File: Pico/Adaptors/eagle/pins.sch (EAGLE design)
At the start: 4 parts

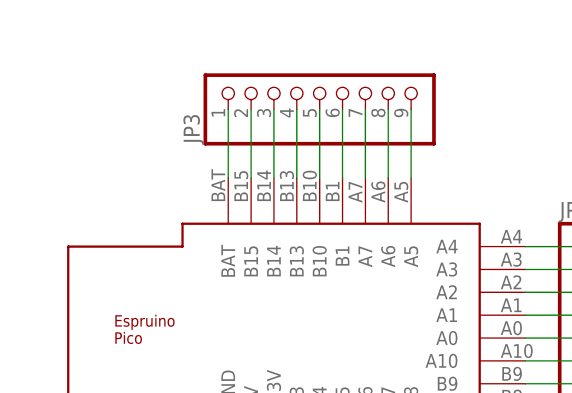
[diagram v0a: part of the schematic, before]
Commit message: add JST connector to pins, update thumbnails
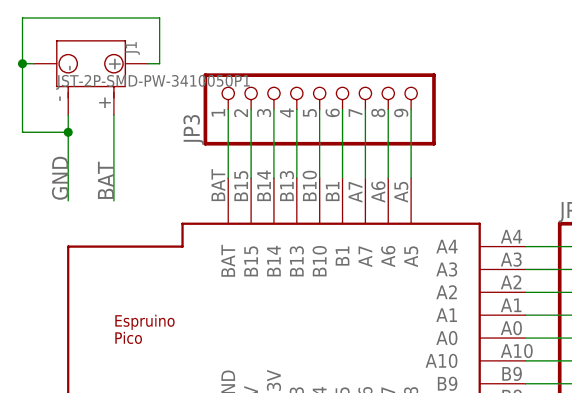
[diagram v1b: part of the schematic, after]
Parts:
- added J1: JST-2P-SMD-PW-3410050P1, OPL Eagle Library:JST-2P-SMD-PW-3410050P1
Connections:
- removed net N$15: JP3.1, U$1.BAT
- new net BAT: J1.+, JP3.1, U$1.BAT
- net GND: now also J1.-, J1.3, J1.4
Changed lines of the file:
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@@
 <layers>
 <layer number="1" name="Top" color="4" fill="1" visible="no" active="no"/>
+<layer number="2" name="Route2" color="1" fill="3" visible="no" active="no"/>
+<layer number="15" name="Route15" color="4" fill="6" visible="no" active="no"/>
 <layer number="16" name="Bottom" color="1" fill="1" visible="no" active="no"/>
 <layer number="17" name="Pads" color="2" fill="1" visible="no" active="no"/>
@@
 <layer number="48" name="Document" color="7" fill="1" visible="no" active="no"/>
 <layer number="49" name="Reference" color="7" fill="1" visible="no" active="no"/>
+<layer number="50" name="dxf" color="7" fill="1" visible="no" active="no"/>
 <layer number="51" name="tDocu" color="7" fill="1" visible="no" active="no"/>
 <layer number="52" name="bDocu" color="7" fill="1" visible="no" active="no"/>
+<layer number="53" name="tGND_GNDA" color="7" fill="9" visible="no" active="no"/>
+<layer number="54" name="bGND_GNDA" color="1" fill="9" visible="no" active="no"/>
+<layer number="56" name="wert" color="7" fill="1" visible="no" active="no"/>
 <layer number="91" name="Nets" color="2" fill="1" visible="yes" active="yes"/>
 <layer number="92" name="Busses" color="1" fill="1" visible="yes" active="yes"/>
@@
 <layer number="97" name="Info" color="7" fill="1" visible="yes" active="yes"/>
 <layer number="98" name="Guide" color="6" fill="1" visible="yes" active="yes"/>
+<layer number="100" name="Muster" color="7" fill="1" visible="no" active="no"/>
+<layer number="101" name="Patch_Top" color="12" fill="4" visible="no" active="no"/>
+<layer number="102" name="Vscore" color="7" fill="1" visible="no" active="no"/>
+<layer number="103" name="tMap" color="7" fill="1" visible="no" active="no"/>
+<layer number="104" name="Name" color="7" fill="1" visible="no" active="no"/>
+<layer number="105" name="tPlate" color="7" fill="1" visible="no" active="no"/>
+<layer number="106" name="bPlate" color="7" fill="1" visible="no" active="no"/>
+<layer number="107" name="Crop" color="7" fill="1" visible="no" active="no"/>
+<layer number="108" name="fp8" color="7" fill="1" visible="no" active="no"/>
+<layer number="109" name="fp9" color="7" fill="1" visible="no" active="no"/>
+<layer number="110" name="110" color="7" fill="1" visible="no" active="no"/>
+<layer number="111" name="111" color="7" fill="1" visible="no" active="no"/>
+<layer number="112" name="tSilk" color="7" fill="1" visible="no" active="no"/>
+<layer number="116" name="Patch_BOT" color="9" fill="4" visible="no" active="no"/>
+<layer number="118" name="Rect_Pads" color="7" fill="1" visible="no" active="no"/>
+<layer number="121" name="_tsilk" color="7" fill="1" visible="no" active="no"/>
+<layer number="122" name="_bsilk" color="7" fill="1" visible="no" active="no"/>
+<layer number="123" name="tTestmark" color="7" fill="1" visible="no" active="no"/>
+<layer number="124" name="bTestmark" color="7" fill="1" visible="no" active="no"/>
+<layer number="125" name="_tNames" color="7" fill="1" visible="no" active="no"/>
+<layer number="126" name="_bNames" color="7" fill="1" visible="no" active="no"/>
+<layer number="127" name="_tValues" color="7" fill="1" visible="no" active="no"/>
+<layer number="128" name="_bValues" color="7" fill="1" visible="no" active="no"/>
+<layer number="131" name="tAdjust" color="7" fill="1" visible="no" active="no"/>
+<layer number="132" name="bAdjust" color="7" fill="1" visible="no" active="no"/>
+<layer number="144" name="DrillLegend" color="7" fill="1" visible="no" active="no"/>
+<layer number="151" name="HeatSink" color="14" fill="1" visible="no" active="no"/>
+<layer number="152" name="_bDocu" color="7" fill="1" visible="no" active="no"/>
+<layer number="199" name="Contour" color="7" fill="1" visible="no" active="no"/>
+<layer number="200" name="200bmp" color="1" fill="10" visible="no" active="no"/>
+<layer number="201" name="201bmp" color="2" fill="1" visible="no" active="no"/>
+<layer number="202" name="202bmp" color="3" fill="1" visible="no" active="no"/>
+<layer number="203" name="203bmp" color="4" fill="10" visible="no" active="no"/>
+<layer number="204" name="204bmp" color="5" fill="10" visible="no" active="no"/>
+<layer number="205" name="205bmp" color="6" fill="10" visible="no" active="no"/>
+<layer number="206" name="206bmp" color="7" fill="10" visible="no" active="no"/>
+<layer number="207" name="207bmp" color="15" fill="10" visible="no" active="no"/>
+<layer number="208" name="208bmp" color="9" fill="10" visible="no" active="no"/>
+<layer number="209" name="209bmp" color="7" fill="1" visible="no" active="no"/>
+<layer number="210" name="210bmp" color="7" fill="1" visible="no" active="no"/>
+<layer number="211" name="211bmp" color="7" fill="1" visible="no" active="no"/>
+<layer number="212" name="212bmp" color="7" fill="1" visible="no" active="no"/>
+<layer number="213" name="213bmp" color="7" fill="1" visible="no" active="no"/>
+<layer number="214" name="214bmp" color="7" fill="1" visible="no" active="no"/>
+<layer number="215" name="215bmp" color="7" fill="1" visible="no" active="no"/>
+<layer number="216" name="216bmp" color="7" fill="1" visible="no" active="no"/>
+<layer number="217" name="217bmp" color="18" fill="1" visible="no" active="no"/>
+<layer number="218" name="218bmp" color="19" fill="1" visible="no" active="no"/>
+<layer number="219" name="219bmp" color="20" fill="1" visible="no" active="no"/>
+<layer number="220" name="220bmp" color="21" fill="1" visible="no" active="no"/>
+<layer number="221" name="221bmp" color="22" fill="1" visible="no" active="no"/>
+<layer number="222" name="222bmp" color="23" fill="1" visible="no" active="no"/>
+<layer number="223" name="223bmp" color="24" fill="1" visible="no" active="no"/>
+<layer number="224" name="224bmp" color="25" fill="1" visible="no" active="no"/>
+<layer number="248" name="Housing" color="7" fill="1" visible="no" active="no"/>
+<layer number="249" name="Edge" color="7" fill="1" visible="no" active="no"/>
+<layer number="250" name="Descript" color="3" fill="1" visible="no" active="no"/>
+<layer number="251" name="SMDround" color="12" fill="11" visible="no" active="no"/>
+<layer number="254" name="OrgLBR" color="13" fill="1" visible="no" active="no"/>
 </layers>
 <schematic xreflabel="%F%N/%S.%C%R" xrefpart="/%S.%C%R">
@@
 <part name="JP3" library="pinhead-2" deviceset="PINHD-1X09" device="_2.54-S"/>
 <part name="JP4" library="pinhead-2" deviceset="PINHD-1X09" device="_2.54-S"/>
+<part name="J1" library="OPL Eagle Library" deviceset="JST-2P-SMD-PW" device="-3410050P1"/>
 </parts>
 <sheets>
@@
 <instance part="JP3" gate="A" x="40.64" y="38.1" rot="R90"/>
 <instance part="JP4" gate="A" x="40.64" y="-17.78" rot="MR270"/>
+<instance part="J1" gate="J" x="15.24" y="40.64" rot="R270"/>
 </instances>
 <busses>
@@
 <wire x1="30.48" y1="-5.08" x2="30.48" y2="-15.24" width="0.1524" layer="91"/>
 </segment>
+<segment>
+<wire x1="21.59" y1="40.64" x2="22.86" y2="40.64" width="0.1524" layer="91"/>
+<wire x1="22.86" y1="40.64" x2="22.86" y2="45.72" width="0.1524" layer="91"/>
+<wire x1="12.7" y1="34.925" x2="12.7" y2="33.02" width="0.1524" layer="91"/>
+<wire x1="12.7" y1="33.02" x2="12.7" y2="25.4" width="0.1524" layer="91"/>
+<wire x1="8.89" y1="40.64" x2="7.62" y2="40.64" width="0.1524" layer="91"/>
+<wire x1="7.62" y1="40.64" x2="7.62" y2="33.02" width="0.1524" layer="91"/>
+<wire x1="7.62" y1="33.02" x2="12.7" y2="33.02" width="0.1524" layer="91"/>
+<wire x1="22.86" y1="45.72" x2="7.62" y2="45.72" width="0.1524" layer="91"/>
+<wire x1="7.62" y1="45.72" x2="7.62" y2="40.64" width="0.1524" layer="91"/>
+<junction x="12.7" y="33.02"/>
+<junction x="7.62" y="40.64"/>
+<label x="12.7" y="25.4" size="1.778" layer="95" rot="R90"/>
+<pinref part="J1" gate="J" pin="-"/>
+<pinref part="J1" gate="J" pin="3"/>
+<pinref part="J1" gate="J" pin="4"/>
+</segment>
 </net>
 <net name="N$9" class="0">
@@
 </segment>
 </net>
-<net name="N$15" class="0">
+<net name="BAT" class="0">
 <segment>
 <pinref part="U$1" gate="G$1" pin="BAT"/>
@@
 <wire x1="30.48" y1="27.94" x2="30.48" y2="35.56" width="0.1524" layer="91"/>
 </segment>
-</net>
+<segment>
+<label x="17.78" y="25.4" size="1.778" layer="95" rot="R90"/>
+<pinref part="J1" gate="J" pin="+"/>
+<wire x1="17.78" y1="34.925" x2="17.78" y2="25.4" width="0.1524" layer="91"/>
+</segment>
+</net>

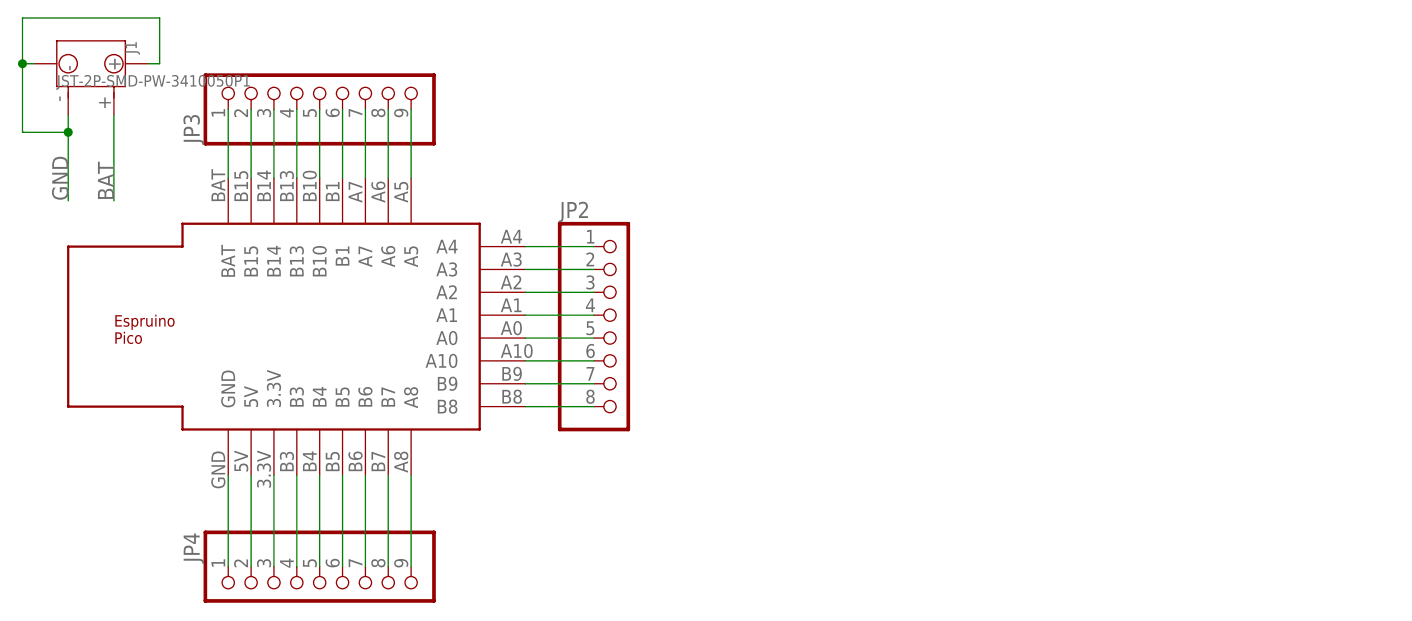
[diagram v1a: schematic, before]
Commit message: Added battery charger pads to proto headers
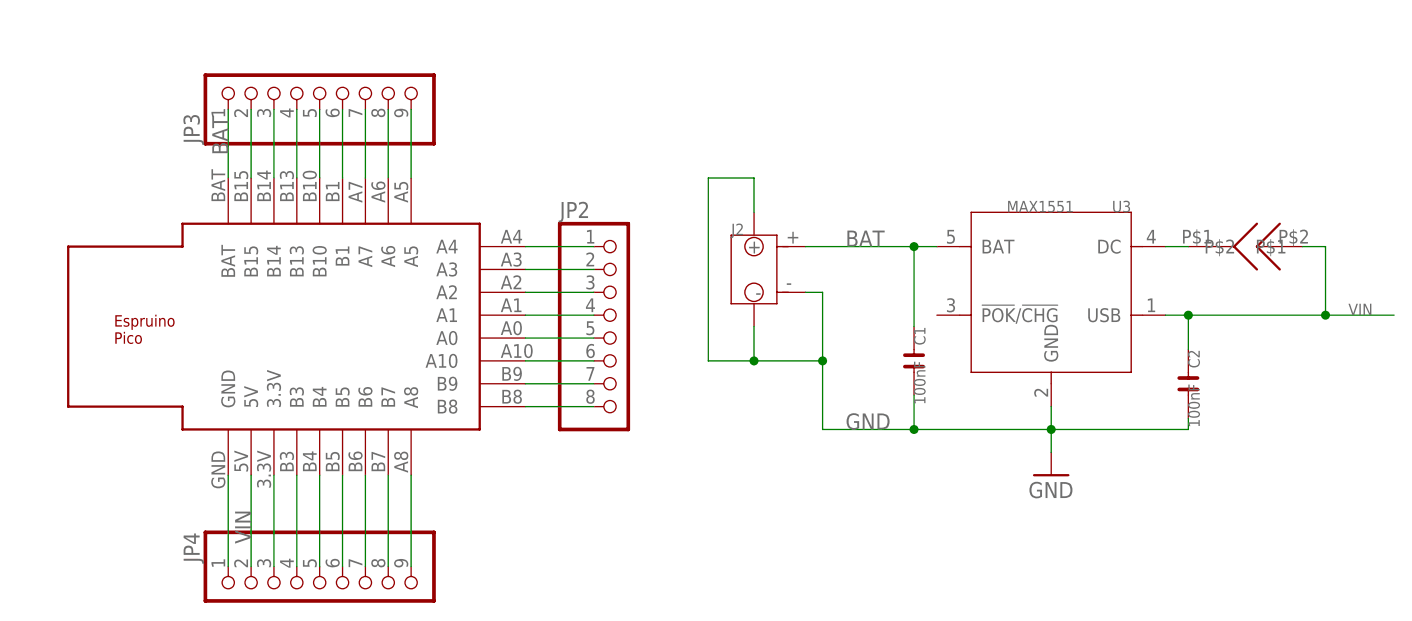
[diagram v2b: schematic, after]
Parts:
- removed J1: JST-2P-SMD-PW-3410050P1, OPL Eagle Library:JST-2P-SMD-PW-3410050P1
- added C1, C2: 100nF, OPL5:C-0603
- added J2: JST-2P-SMD-PW-3410050P1, OPL Eagle Library:JST-2P-SMD-PW-3410050P1
- added U$4: SOLDERJUMPER, solder_jumper:SOLDERJUMPER
- added U3: MAX1551, template:MAX1551
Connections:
- removed net 5V: JP4.2, U$1.5V
- new net N$15: U$4.P$1, U3.DC
- new net VIN: C2.1, JP4.2, U$1.5V, U$4.P$2, U3.USB
- net BAT: now also C1.1, J2.+, U3.BAT; no longer J1.+
- net GND: now also C1.2, C2.2, J2.-, J2.3, J2.4, U3.GND; no longer J1.-, J1.3, J1.4
